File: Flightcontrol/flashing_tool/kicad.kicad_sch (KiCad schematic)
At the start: 16 parts, among them J1 2171790001, J2 Conn_01x03_Pin, J3 Conn_01x03_Pin, U1 ESP32-S3-WROOM-1U-N16R8

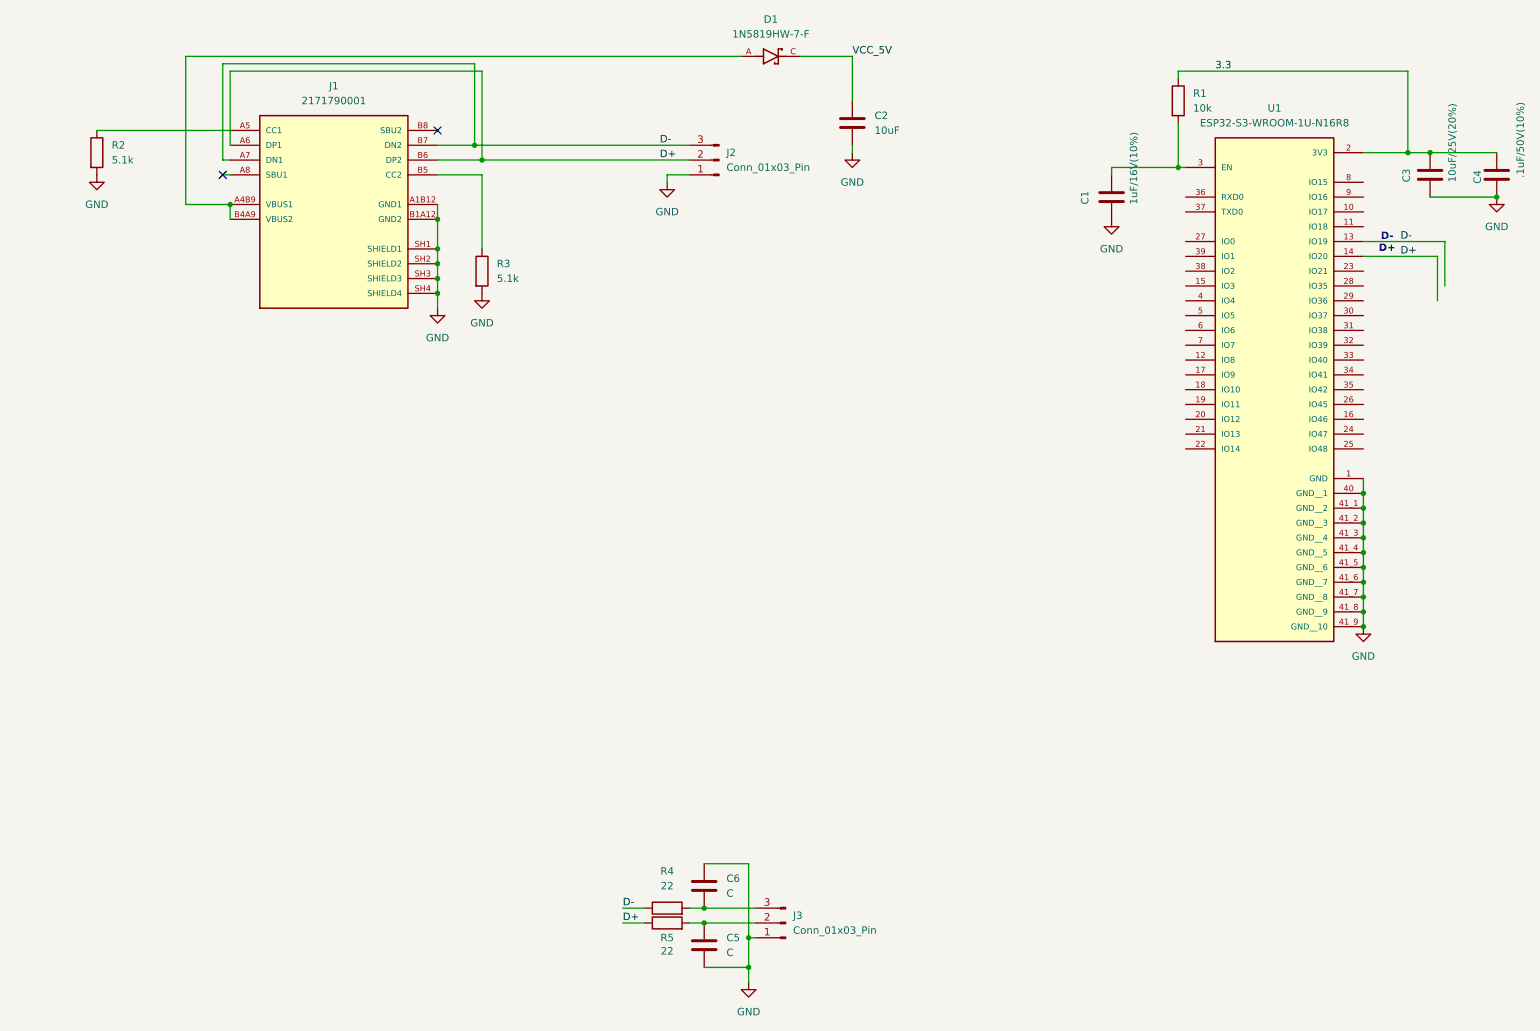
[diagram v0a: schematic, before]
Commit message: moved flash tool to seperate kicad file
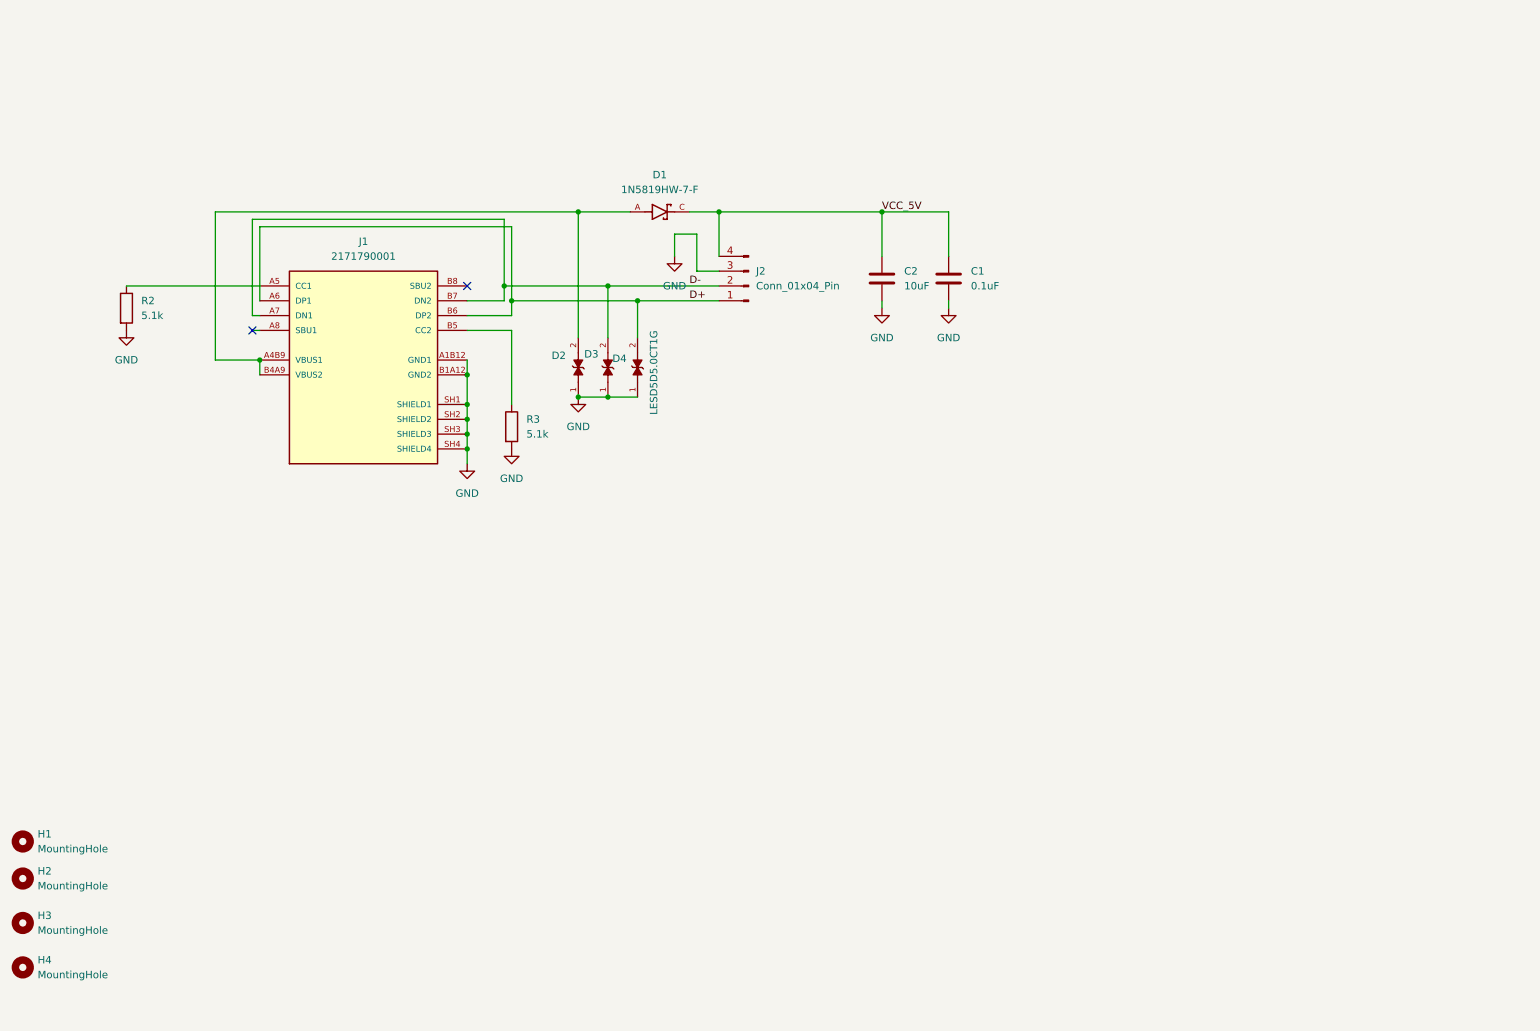
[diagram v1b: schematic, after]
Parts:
- removed C3: 10uF/25V(20%), symbol Device:C
- removed C4: .1uF/50V(10%), symbol Device:C
- removed C5, C6: C, symbol Device:C
- removed J2, J3: Conn_01x03_Pin, symbol Connector:Conn_01x03_Pin
- removed R1: 10k, symbol Device:R
- removed R4, R5: 22, symbol Device:R
- removed U1: ESP32-S3-WROOM-1U-N16R8, ESP32-S3-WROOM-1U-N16R8:XCVR_ESP32-S3-WROOM-1U-N16R8, symbol ESP32-S3-WROOM-1U-N16R8:ESP32-S3-WROOM-1U-N16R8
- added D2, D3, D4: LESD5D5.0CT1G, LESD5D5.0CT1G:TVS_LESD5D5.0CT1G, symbol LESD5D5.0CT1G:LESD5D5.0CT1G
- added H1, H2, H3, H4: MountingHole, MountingHole:MountingHole_3.2mm_M3, symbol Mechanical:MountingHole
- added J2: Conn_01x04_Pin, Connector_PinHeader_2.54mm:PinHeader_1x04_P2.54mm_Vertical, symbol Connector:Conn_01x04_Pin
- C1: value 1uF/16V(10%) -> 0.1uF; footprint (none) -> Capacitor_SMD:C_0201_0603Metric
- C2: footprint (none) -> Capacitor_SMD:C_0201_0603Metric
- D1: footprint 1N5819HW-7-F:SOD3715X145N -> 1N5819HW_7_F:SOD3715X145N
- R2, R3: footprint (none) -> Resistor_SMD:R_0201_0603Metric
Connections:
- net D+: now also D4.2, J2.1 (Pin_1)
- net D-: now also D3.2, J2.2 (Pin_2)
- net GND: now also D2.1, D3.1, D4.1, J2.3 (Pin_3)
- net VCC_5V: now also C1.1, J2.4 (Pin_4)
- net at D1.A, J1.A4B9 (VBUS1), J1.B4A9 (VBUS2): now also D2.2
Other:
- note removed: "D- D+"
- moved on the sheet: C2, D1, J1, R2, R3

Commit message: flasher4otg V1 finished
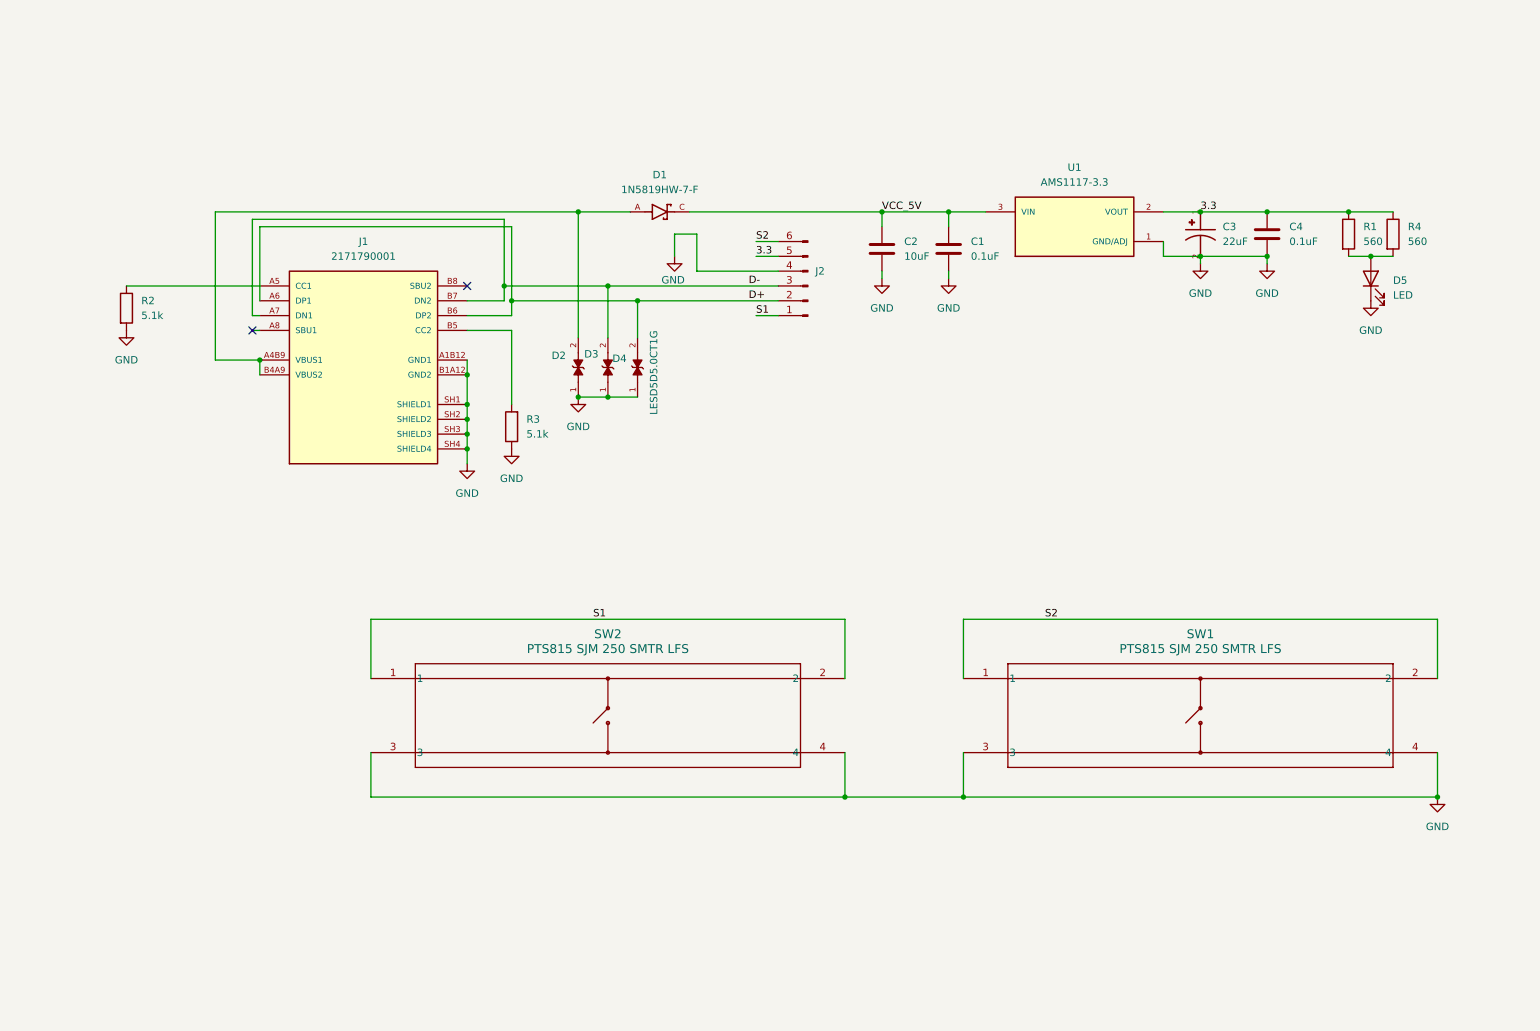
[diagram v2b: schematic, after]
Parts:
- removed H1, H2, H3, H4: MountingHole, MountingHole:MountingHole_3.2mm_M3, symbol Mechanical:MountingHole
- removed J2: Conn_01x04_Pin, Connector_PinHeader_2.54mm:PinHeader_1x04_P2.54mm_Vertical, symbol Connector:Conn_01x04_Pin
- added C3: 22uF, TAJA226K010RNJ:CAPMP3216X180N, symbol TAJA226K010RNJ:TAJA226K010RNJ
- added C4: 0.1uF, Capacitor_SMD:C_0603_1608Metric, symbol Device:C
- added D5: LED, LED_SMD:LED_0603_1608Metric, symbol Device:LED
- added J2: Conn_01x06_Pin, Connector_PinHeader_2.54mm:PinHeader_1x06_P2.54mm_Vertical, symbol Connector:Conn_01x06_Pin
- added R1, R4: 560, Resistor_SMD:R_0805_2012Metric, symbol Device:R
- added SW1, SW2: PTS815 SJM 250 SMTR LFS, GSPTS0020:GSPTS0020, symbol GSPTS0020:PTS815_SJM_250_SMTR_LFS
- added U1: AMS1117-3.3, AMS1117-3.3:SOT229P700X180-4N, symbol AMS1117-3.3:AMS1117-3.3
- C1, C2: footprint Capacitor_SMD:C_0201_0603Metric -> Capacitor_SMD:C_0603_1608Metric
- R2, R3: footprint Resistor_SMD:R_0201_0603Metric -> Resistor_SMD:R_0603_1608Metric
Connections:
- net D+: now also J2.2 (Pin_2)
- net D-: now also J2.3 (Pin_3)
- net GND: now also R3.1, C3.2, C4.2, D5.1 (K), J2.4 (Pin_4), SW1.3, SW1.4, SW2.3, SW2.4, U1.1 (GND/ADJ); no longer R3.2
- net VCC_5V: now also U1.3 (VIN)
- net at J1.B5 (CC2): now also R3.2; no longer R3.1
- new net: D5.2 (A), R1.2, R4.2
- new net 3.3: C3.1, C4.1, J2.5 (Pin_5), R1.1, R4.1, U1.2 (VOUT)
- new net S1: J2.1 (Pin_1), SW2.1, SW2.2
- new net S2: J2.6 (Pin_6), SW1.1, SW1.2
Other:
- moved on the sheet: C1, C2, R3
